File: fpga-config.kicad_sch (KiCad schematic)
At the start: 7 parts, among them U1 MPFS250T-FCVG484, Y3 Oscillator_125MHz_DSC1103DI2

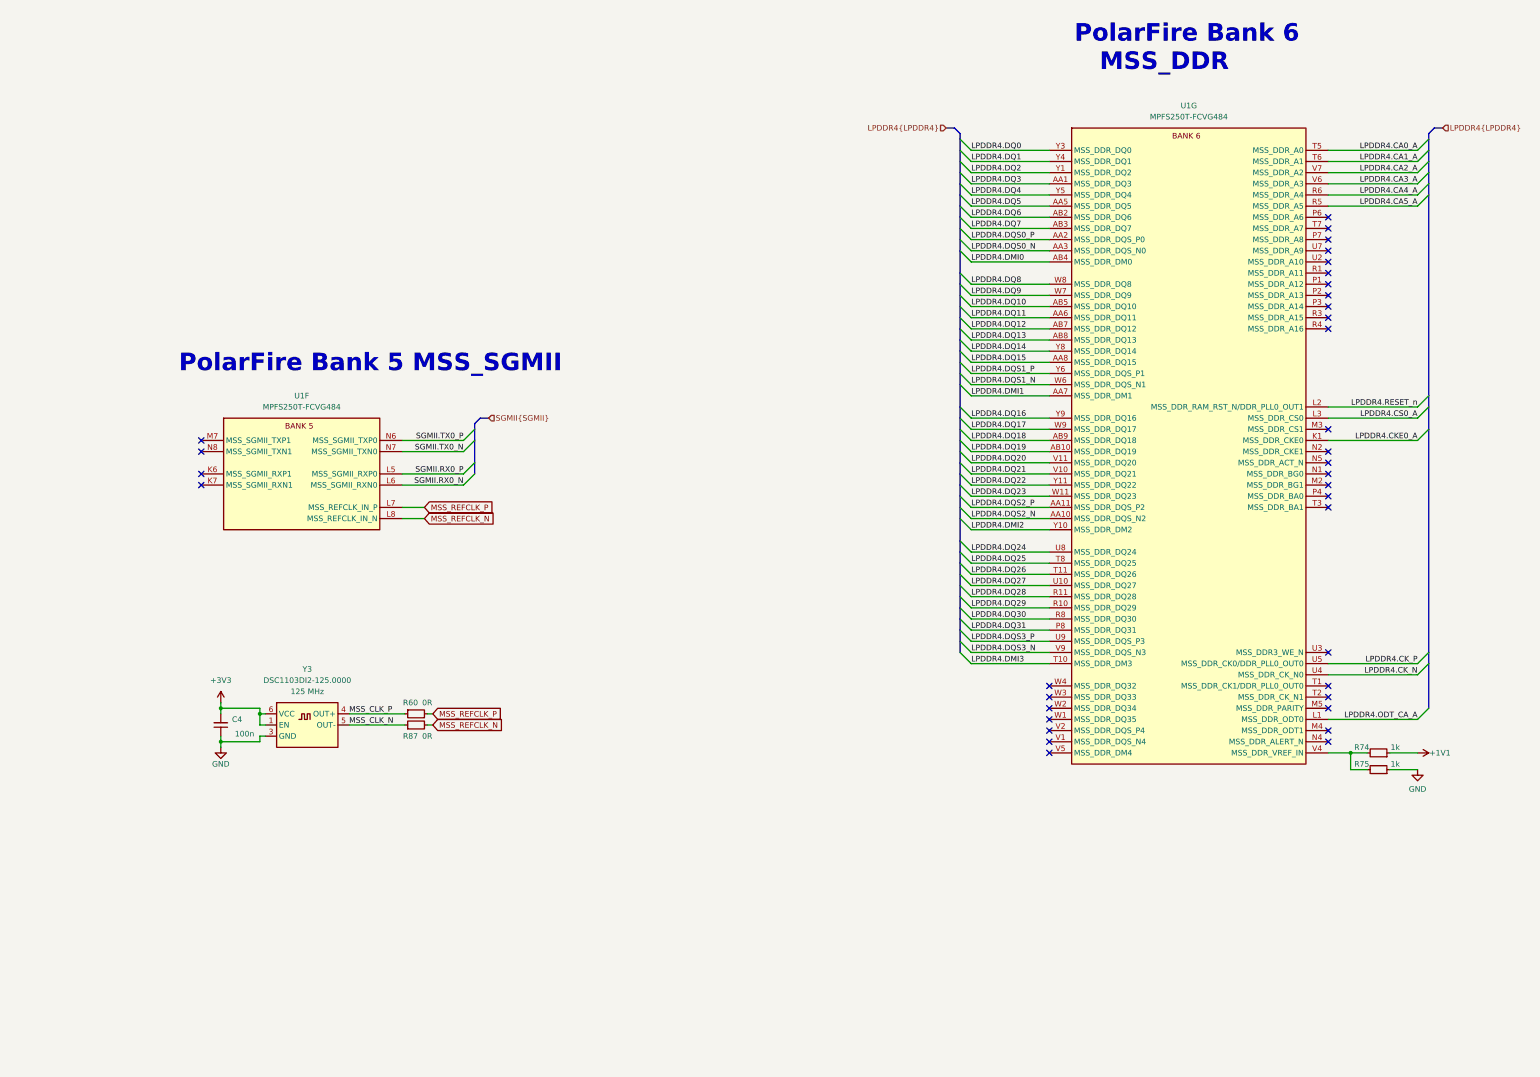
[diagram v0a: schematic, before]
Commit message: [#57505] Continue migration to hierarchical schematic
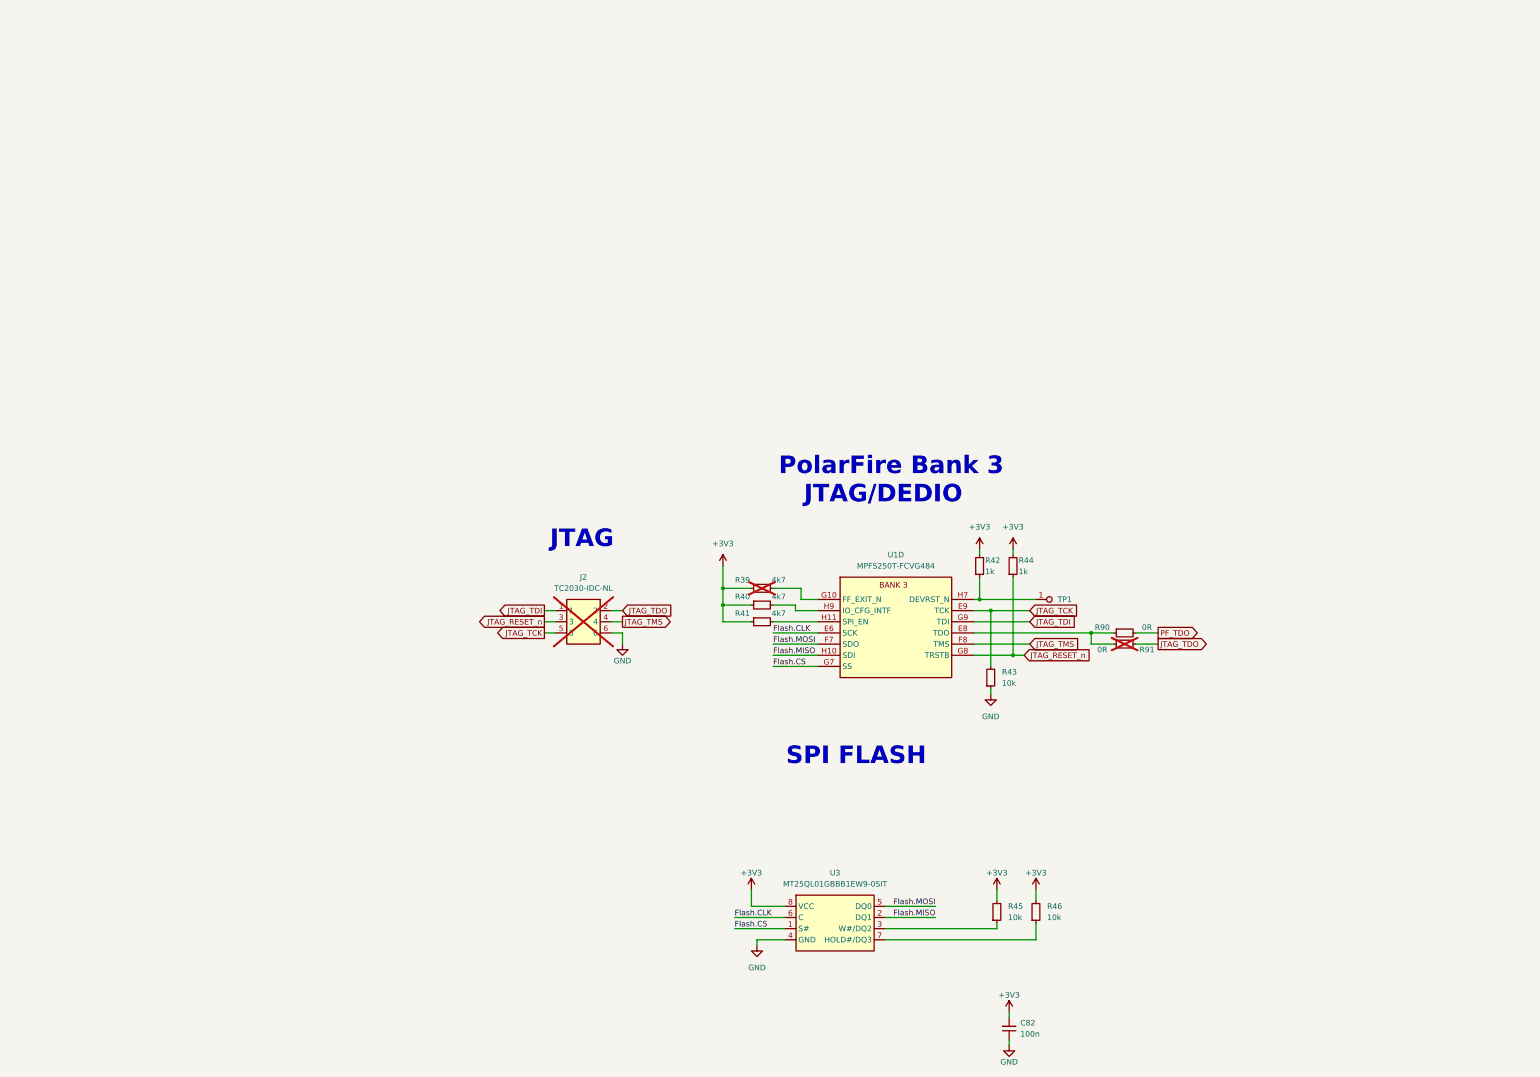
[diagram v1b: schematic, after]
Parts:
- removed C4: C_100n_0402, antmicro-footprints:C_0402_1005Metric, symbol antmicroCapacitors0402:C_100n_0402
- removed R60, R87: R_0R_0402, antmicro-footprints:R_0402_1005Metric, symbol antmicroResistors0402:R_0R_0402
- removed R74, R75: R_1k_0402, antmicro-footprints:R_0402_1005Metric, symbol antmicroResistors0402:R_1k_0402
- removed U1: MPFS250T-FCVG484, antmicro-footprints:BGA-484_19x19mm_Layout22x22_P0.8mm-microchip-technology-mpfs250t-fcvg484, symbol antmicroFPGAChips:MPFS250T-FCVG484
- removed Y3: Oscillator_125MHz_DSC1103DI2, antmicro-footprints:Oscillator_SMD_Microchip_DSC1103DI2_2.5x2x0.85mm, symbol antmicroOscillators:Oscillator_125MHz_DSC1103DI2
- added C82: C_100n_0402, antmicro-footprints:C_0402_1005Metric, symbol antmicroCapacitors0402:C_100n_0402
- added J2: Tag-Connect_TC2030-IDC-NL_2x3_P1.27mm, antmicro-footprints:Tag-Connect_TC2030-IDC-NL_2x3_P1.27mm, symbol antmicroTestPoints:Tag-Connect_TC2030-IDC-NL_2x3_P1.27mm
- added R39, R40, R41: R_4k7_0402, antmicro-footprints:R_0402_1005Metric, symbol antmicroResistors0402:R_4k7_0402
- added R42, R44: R_1k_0402, antmicro-footprints:R_0402_1005Metric, symbol antmicroResistors0402:R_1k_0402
- added R43, R45, R46: R_10k_0402, antmicro-footprints:R_0402_1005Metric, symbol antmicroResistors0402:R_10k_0402
- added R90, R91: R_0R_0402, antmicro-footprints:R_0402_1005Metric, symbol antmicroResistors0402:R_0R_0402
- added TP1: TP_0.75mm_SMD, antmicro-footprints:TP_SMD_0.75mm, symbol antmicroTestPoints:TP_0.75mm_SMD
- added U1: MPFS250T-FCVG484, antmicro-footprints:BGA-484_19x19mm_Layout22x22_P0.8mm-microchip-technology-mpfs250t-fcvg484, symbol antmicroFPGAChips:MPFS250T-FCVG484
- added U3: MT25QL01GBBB1EW9-0SIT, antmicro-footprints:W-PDFN-8-1EP_8x6mm_P1.27mm_EP4.3x3.4mm, symbol antmicroMemory:MT25QL01GBBB1EW9-0SIT
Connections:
- net +3V3: now also C82.2, R39.1, R40.1, R41.1, R42.2, R44.2, R45.2, R46.2, U3.8 (VCC)
- net GND: now also C82.1, J2.6, R43.1, U3.4 (GND)
- new net: R45.1, U3.3 (W#/DQ2)
- new net: R46.1, U3.7 (HOLD#/DQ3)
- new net: R90.1, R91.2, U1.E8 (TDO)
- new net: R39.2, U1.G10 (FF_EXIT_N)
- new net: R41.2, U1.H11 (SPI_EN)
- new net: R42.1, TP1.1, U1.H7 (DEVRST_N)
- new net: R40.2, U1.H9 (IO_CFG_INTF)
- new net Flash.CLK: U1.E6 (SCK), U3.6 (C)
- new net Flash.CS: U1.G7 (SS), U3.1 (S#)
- new net Flash.MISO: U1.H10 (SDI), U3.2 (DQ1)
- new net Flash.MOSI: U1.F7 (SDO), U3.5 (DQ0)
- new net JTAG_RESET_n: J2.3, R44.1, U1.G8 (TRSTB)
- new net JTAG_TCK: J2.5, R43.2, U1.E9 (TCK)
- new net JTAG_TDI: J2.1, U1.G9 (TDI)
- new net JTAG_TDO: J2.2, R91.1
- new net JTAG_TMS: J2.4, U1.F8 (TMS)
- new net PF_TDO: R90.2
- no-connect marks 35 -> 0
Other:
- note added: "JTAG"
- note added: "PolarFire Bank 3 JTAG/DEDIO"
- note added: "SPI FLASH"
- note removed: "PolarFire Bank 5 MSS_SGMII"
- note removed: "PolarFire Bank 6 MSS_DDR"

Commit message: [#57422] Finishing touches
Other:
- moved on the sheet: C82, J2, R39, R40, R41, R42, R43, R44, R45, R46, R90, R91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

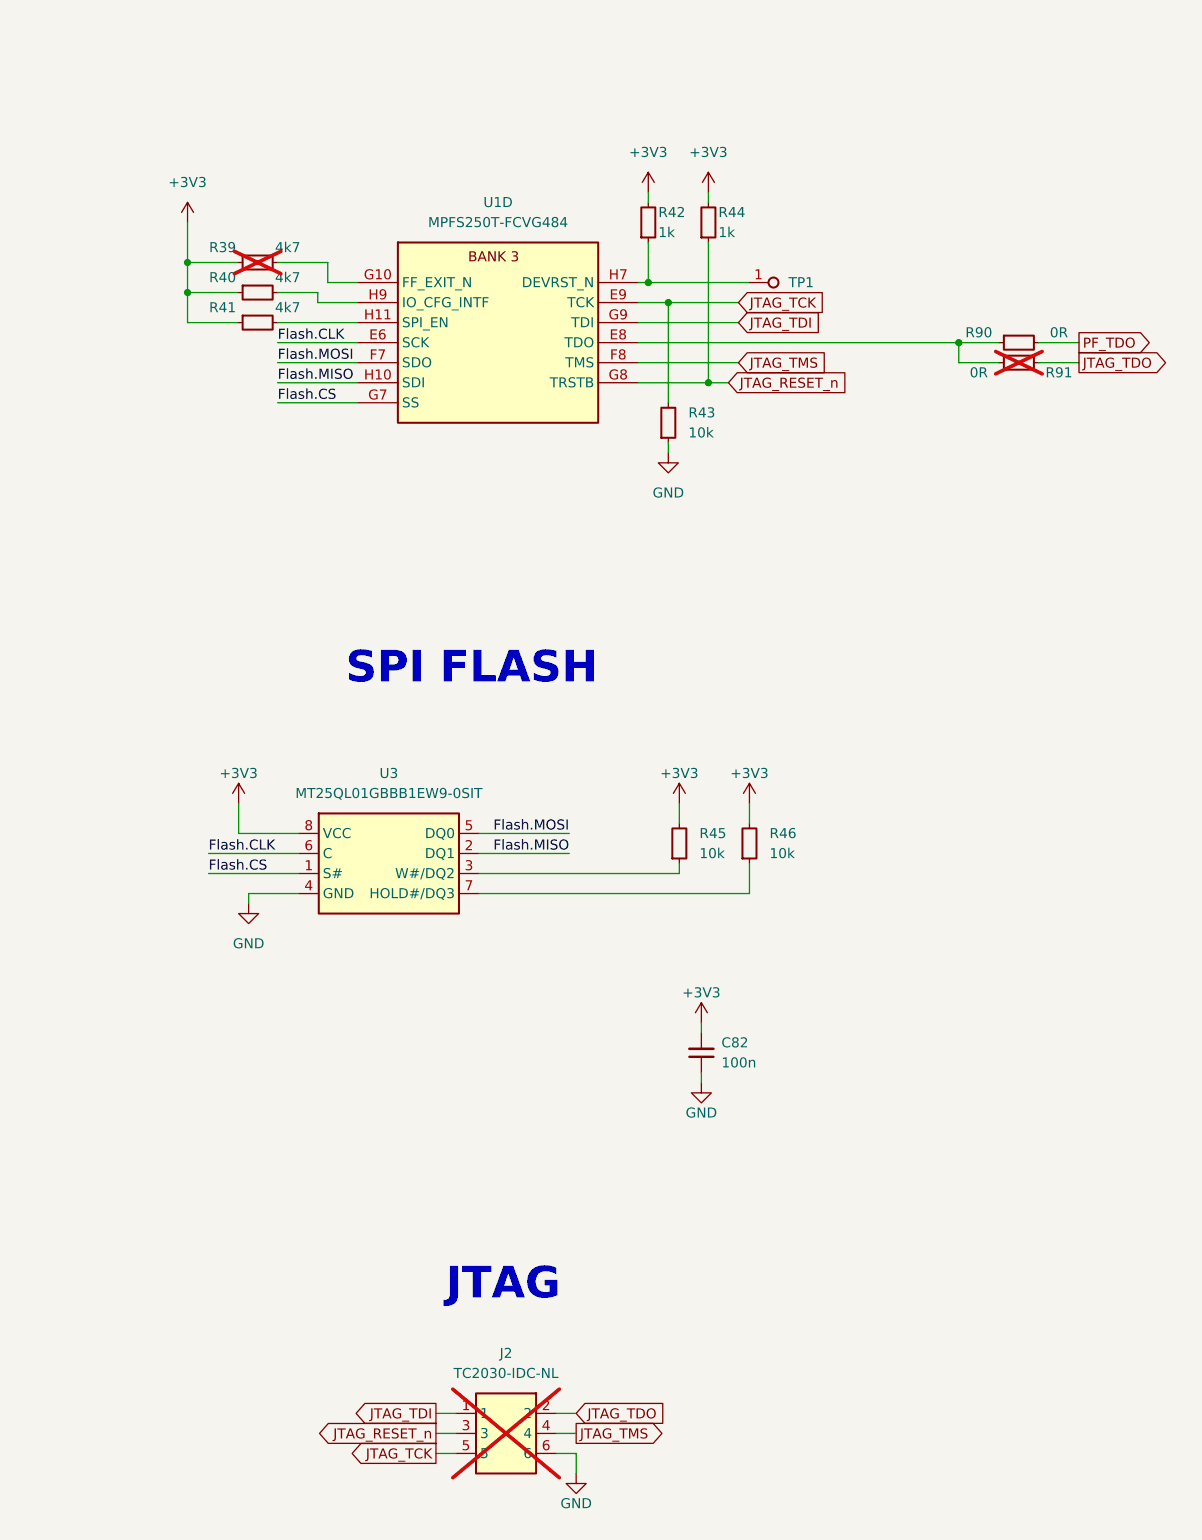
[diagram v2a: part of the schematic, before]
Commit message: [#57422] Align schematics
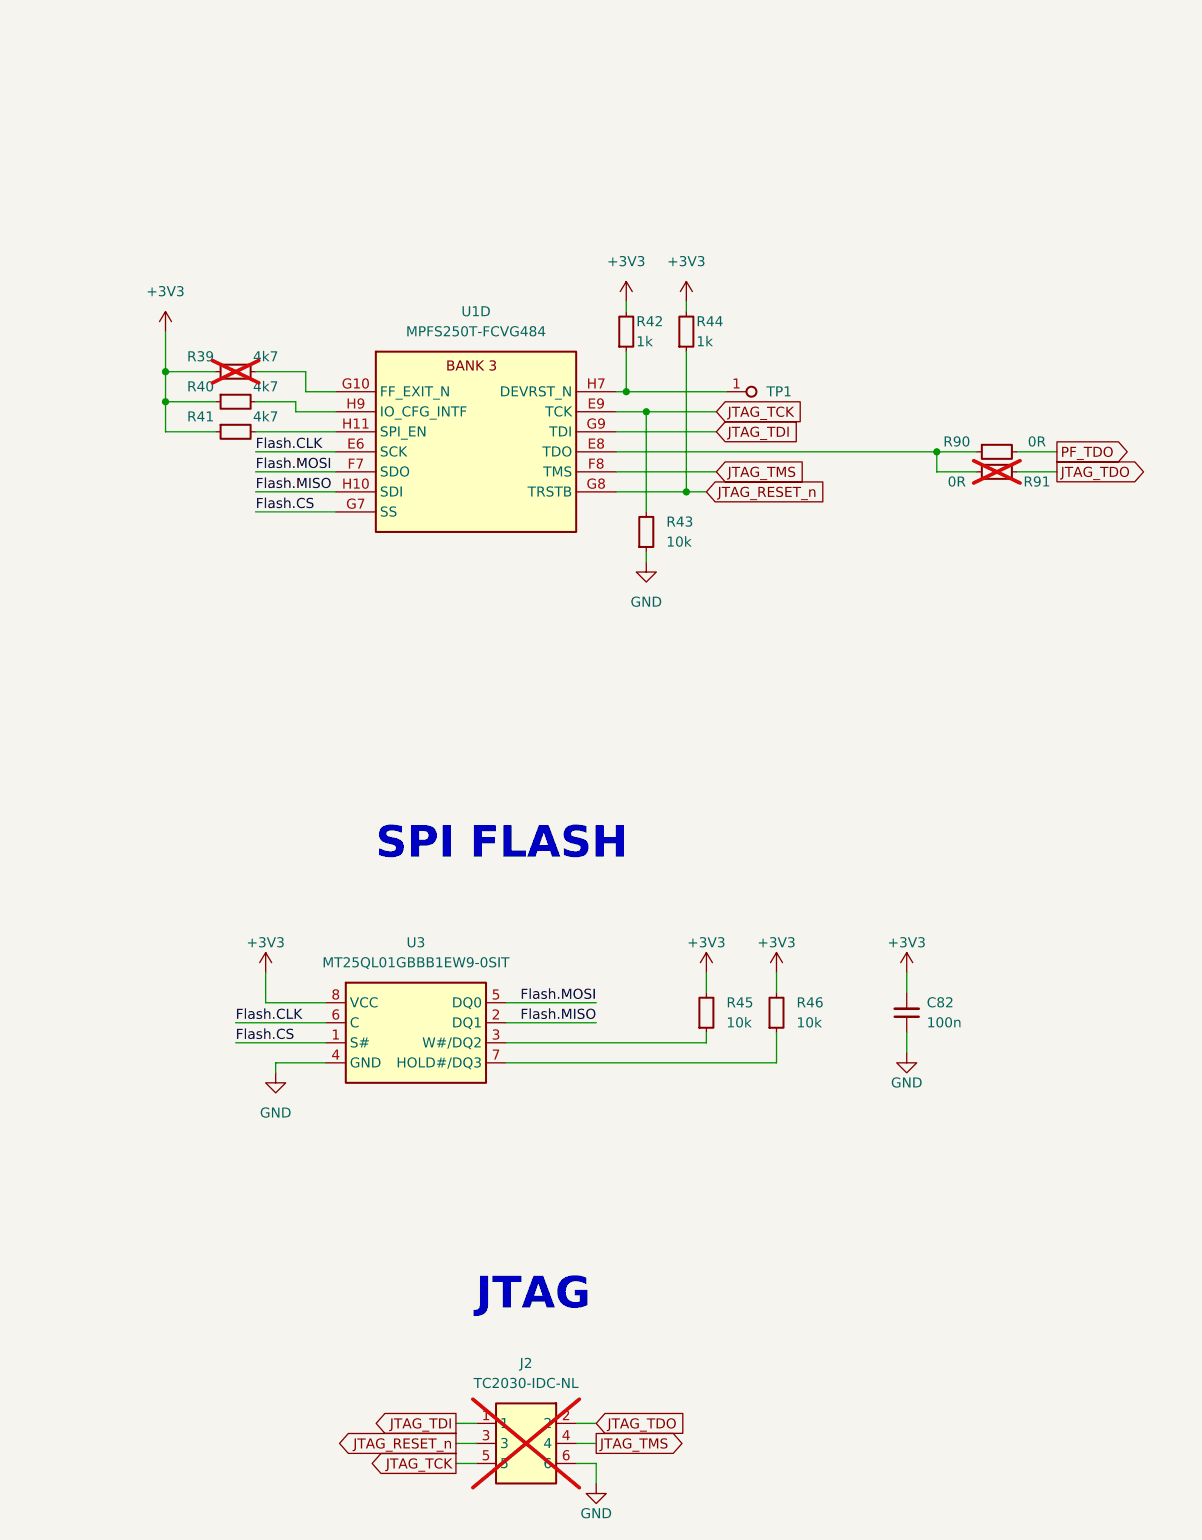
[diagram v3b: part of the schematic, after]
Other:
- moved on the sheet: C82, J2, R39, R40, R41, R42, R43, R44, R45, R46, R90, R91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

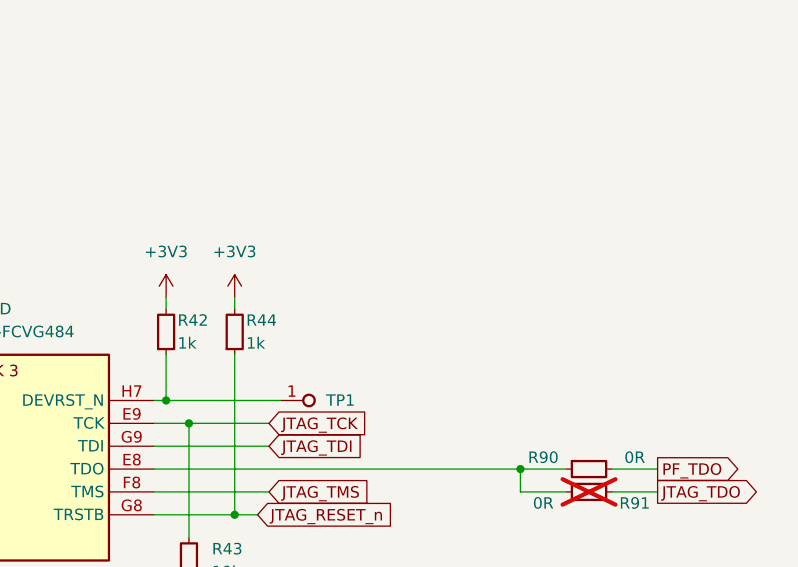
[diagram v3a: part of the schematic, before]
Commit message: [#59910] Add +3V3 testpoint near Tag-Connect
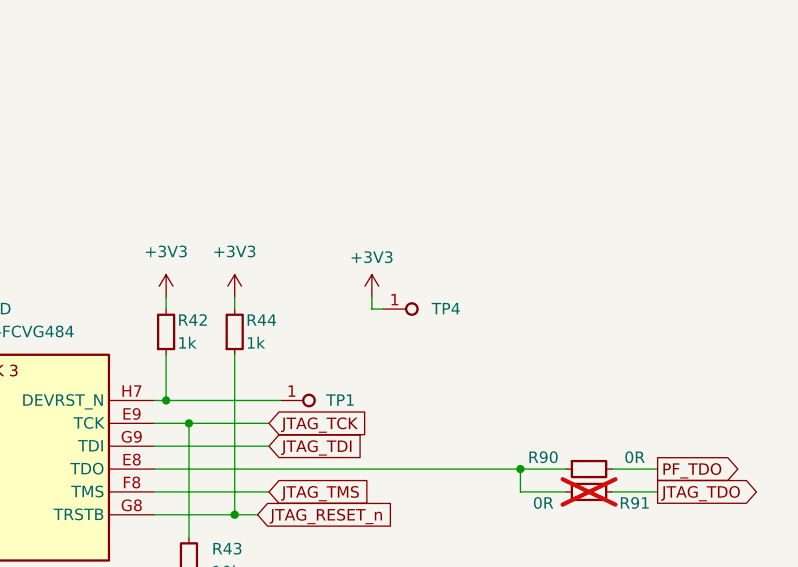
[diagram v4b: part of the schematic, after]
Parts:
- added TP4: TP_0.75mm_SMD, antmicro-footprints:TP_SMD_0.75mm, symbol antmicroTestPoints:TP_0.75mm_SMD
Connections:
- net +3V3: now also TP4.1
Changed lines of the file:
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@@
+    (stroke (width 0) (type default))
+  )
+  (wire (pts (xy 240.03 76.2) (xy 240.03 74.93))
     (stroke (width 0) (type default))
   )
   (wire (pts (xy 175.26 88.9) (xy 180.34 88.9))
+    (stroke (width 0) (type default))
+  )
+  (wire (pts (xy 240.03 76.2) (xy 241.3 76.2))
     (stroke (width 0) (type default))
   )
@@
         )
       )
+    )
+  )
+  (symbol (lib_id "antmicroTestPoints:TP_0.75mm_SMD") (at 241.3 76.2 0) (unit 1)
+    (in_bom no) (on_board yes) (dnp no)
+    (property "Reference" "TP4" (at 248.285 76.2 0)
+      (effects (font (size 1.27 1.27) (thickness 0.15)))
+    )
+    (property "Value" "TP_0.75mm_SMD" (at 252.095 80.01 0)
+      (effects (font (size 1.27 1.27) (thickness 0.15)) (justify left bottom) hide)
+    )
+    (property "Footprint" "antmicro-footprints:TP_SMD_0.75mm" (at 252.095 82.55 0)
+      (effects (font (size 1.27 1.27) (thickness 0.15)) (justify left bottom) hide)
+    )
+    (property "Datasheet" "" (at 259.08 88.9 0)
+      (effects (font (size 1.27 1.27) (thickness 0.15)) (justify left bottom) hide)
+    )
+    (property "MPN" "" (at 252.095 87.63 0)
+      (effects (font (size 1.27 1.27) (thickness 0.15)) (justify left bottom) hide)
+    )
+    (property "Manufacturer" "" (at 252.095 82.55 0)
+      (effects (font (size 1.27 1.27) (thickness 0.15)) (justify left bottom) hide)
+    )
+    (property "Author" "Antmicro" (at 252.095 85.09 0)
+      (effects (font (size 1.27 1.27) (thickness 0.15)) (justify left bottom) hide)
+    )
+    (property "License" "Apache-2.0" (at 252.095 87.63 0)
+      (effects (font (size 1.27 1.27) (thickness 0.15)) (justify left bottom) hide)
+    )
+    (pin "1")
+    (instances
+      (project "polarfire-som"
+        (path "/db4a0d3e-2eb3-499e-977d-6eb378cfd3ed/dc7a7582-fcf3-450b-b684-8a5b0874bf56"
+          (reference "TP4") (unit 1)
+        )
+      )
+    )
+  )
+  (symbol (lib_id "antmicropower:+3V3") (at 240.03 74.93 0) (unit 1)
+    (in_bom yes) (on_board yes) (dnp no) (fields_autoplaced)
+    (property "Reference" "#PWR0195" (at 255.27 74.93 0)
+      (effects (font (size 1.27 1.27) (thickness 0.15)) (justify left bottom) hide)
+    )
+    (property "Value" "+3V3" (at 240.03 70.485 0)
+      (effects (font (size 1.27 1.27) (thickness 0.15)))
+    )
+    (property "Footprint" "" (at 255.27 82.55 0)
+      (effects (font (size 1.27 1.27) (thickness 0.15)) (justify left bottom) hide)
+    )
+    (property "Datasheet" "" (at 255.27 85.09 0)
+      (effects (font (size 1.27 1.27) (thickness 0.15)) (justify left bottom) hide)
+    )
+    (property "Author" "Antmicro" (at 255.27 77.47 0)
+      (effects (font (size 1.27 1.27) (thickness 0.15)) (justify left bottom) hide)
+    )
+    (property "License" "Apache-2.0" (at 255.27 80.01 0)
+      (effects (font (size 1.27 1.27) (thickness 0.15)) (justify left bottom) hide)
+    )
+    (pin "1")
+    (instances
+      (project "polarfire-som"
+        (path "/db4a0d3e-2eb3-499e-977d-6eb378cfd3ed/dc7a7582-fcf3-450b-b684-8a5b0874bf56"
+          (reference "#PWR0195") (unit 1)
+        )
+      )
